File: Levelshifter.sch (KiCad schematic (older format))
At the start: 7 parts

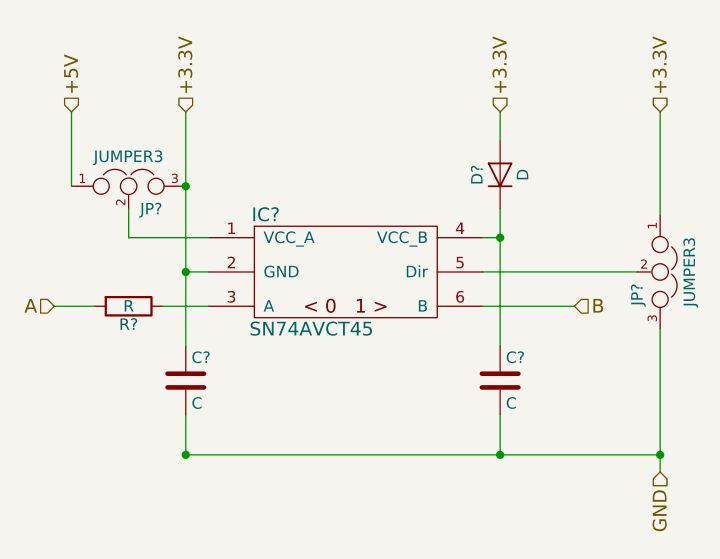
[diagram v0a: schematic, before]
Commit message: Route power, reroute data signals to top layer
Signed-off-by: katie dunne <kedunne@lbl.gov>
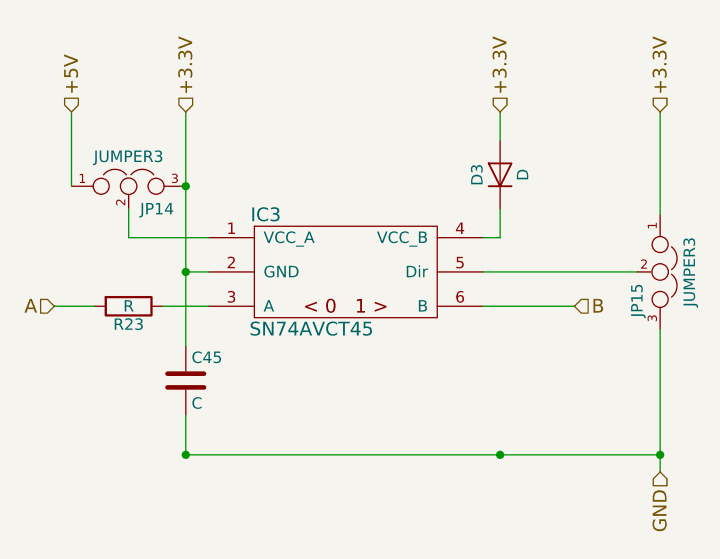
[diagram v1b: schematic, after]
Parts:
- removed C?: C, symbol C
- C43: renamed from C?; footprint (none) -> Capacitors_SMD:C_0805_HandSoldering
- D2: renamed from D?; footprint (none) -> Diodes_SMD:D_0805
- IC2: renamed from IC?; footprint (none) -> TO_SOT_Packages_SMD:SOT-23-6_Handsoldering
- R22: renamed from R?; footprint (none) -> Resistors_SMD:R_0603_HandSoldering
- gave numbers to parts that had none: 2
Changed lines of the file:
@@
 EESchema Schematic File Version 2
+LIBS:vhdci_fei4_rj45-rescue
+LIBS:ds90lv004
+LIBS:con-molex-vhdci
 LIBS:power
 LIBS:device
@@
 $EndDescr
 $Comp
-L JUMPER3 JP?
+L JUMPER3 JP16
 U 1 1 59136121
 P 3825 4150
-F 0 "JP?" H 3875 4050 50  0000 L CNN
+AR Path="/59195600/59136121" Ref="JP16"  Part="1"
+AR Path="/59133F97/59136121" Ref="JP14"  Part="1"
+AR Path="/5919615E/59136121" Ref="JP18"  Part="1"
+F 0 "JP14" H 3875 4050 50  0000 L CNN
 F 1 "JUMPER3" H 3825 4250 50  0000 C BNN
 F 2 "" H 3825 4150 50  0000 C CNN
@@
 $EndComp
 $Comp
-L JUMPER3 JP?
+L JUMPER3 JP17
 U 1 1 5913615C
 P 6150 4525
-F 0 "JP?" H 6200 4425 50  0000 L CNN
+AR Path="/59195600/5913615C" Ref="JP17"  Part="1"
+AR Path="/59133F97/5913615C" Ref="JP15"  Part="1"
+AR Path="/5919615E/5913615C" Ref="JP19"  Part="1"
+F 0 "JP15" H 6200 4425 50  0000 L CNN
 F 1 "JUMPER3" H 6150 4625 50  0000 C BNN
 F 2 "" H 6150 4525 50  0000 C CNN
@@
 $EndComp
 $Comp
-L C C?
+L C C43
 U 1 1 5913620E
 P 4075 5000
-F 0 "C?" H 4100 5100 50  0000 L CNN
+AR Path="/59195600/5913620E" Ref="C43"  Part="1"
+AR Path="/59133F97/5913620E" Ref="C41"  Part="1"
+AR Path="/5919615E/5913620E" Ref="C45"  Part="1"
+F 0 "C45" H 4100 5100 50  0000 L CNN
 F 1 "C" H 4100 4900 50  0000 L CNN
-F 2 "" H 4113 4850 50  0001 C CNN
+F 2 "Capacitors_SMD:C_0805_HandSoldering" H 4113 4850 50  0001 C CNN
 F 3 "" H 4075 5000 50  0001 C CNN
 	1    4075 5000
@@
 $EndComp
 $Comp
-L C C?
-U 1 1 5913623B
-P 5450 5000
-F 0 "C?" H 5475 5100 50  0000 L CNN
-F 1 "C" H 5475 4900 50  0000 L CNN
-F 2 "" H 5488 4850 50  0001 C CNN
-F 3 "" H 5450 5000 50  0001 C CNN
-	1    5450 5000
-	1    0    0    -1
-$EndComp
-$Comp
-L SN74AVCT45 IC?
+L SN74AVCT45 IC2
 U 1 1 591362B4
 P 4825 4525
-F 0 "IC?" H 4425 4775 60  0000 C CNN
+AR Path="/59195600/591362B4" Ref="IC2"  Part="1"
+AR Path="/59133F97/591362B4" Ref="IC1"  Part="1"
+AR Path="/5919615E/591362B4" Ref="IC3"  Part="1"
+F 0 "IC3" H 4425 4775 60  0000 C CNN
 F 1 "SN74AVCT45" H 4625 4275 60  0000 C CNN
-F 2 "" H 4175 4675 60  0001 C CNN
+F 2 "TO_SOT_Packages_SMD:SOT-23-6_Handsoldering" H 4175 4675 60  0001 C CNN
 F 3 "" H 4175 4675 60  0001 C CNN
 	1    4825 4525
@@
 $EndComp
 $Comp
-L R R?
+L R R22
 U 1 1 59136685
 P 3825 4675
-F 0 "R?" V 3905 4675 50  0000 C CNN
+AR Path="/59195600/59136685" Ref="R22"  Part="1"
+AR Path="/59133F97/59136685" Ref="R21"  Part="1"
+AR Path="/5919615E/59136685" Ref="R23"  Part="1"
+F 0 "R23" V 3905 4675 50  0000 C CNN
 F 1 "R" V 3825 4675 50  0000 C CNN
-F 2 "" V 3755 4675 50  0001 C CNN
+F 2 "Resistors_SMD:R_0603_HandSoldering" V 3755 4675 50  0001 C CNN
 F 3 "" H 3825 4675 50  0001 C CNN
 	1    3825 4675
@@
 A
 $Comp
-L D D?
+L D D2
 U 1 1 59136F14
 P 5450 4100
-F 0 "D?" H 5450 4200 50  0000 C CNN
+AR Path="/59195600/59136F14" Ref="D2"  Part="1"
+AR Path="/59133F97/59136F14" Ref="D1"  Part="1"
+AR Path="/5919615E/59136F14" Ref="D3"  Part="1"
+F 0 "D3" H 5450 4200 50  0000 C CNN
 F 1 "D" H 5450 4000 50  0000 C CNN
-F 2 "" H 5450 4100 50  0001 C CNN
+F 2 "Diodes_SMD:D_0805" H 5450 4100 50  0001 C CNN
 F 3 "" H 5450 4100 50  0001 C CNN
 	1    5450 4100
@@
 Wire Wire Line
 	5375 4375 5450 4375
-Connection ~ 5450 4375
-Wire Wire Line
-	5450 5150 5450 5325
 Connection ~ 5450 5325
-Wire Wire Line
-	5450 4250 5450 4850
 Wire Wire Line
 	5375 4525 6050 4525
@@
 	6150 4775 6150 5400
 Connection ~ 6150 5325
+Wire Wire Line
+	5450 4375 5450 4250
 $EndSCHEMATC

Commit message: Route U6, U4, U5
Signed-off-by: Katie Dunne <kdunne@mail.ccsf.edu>
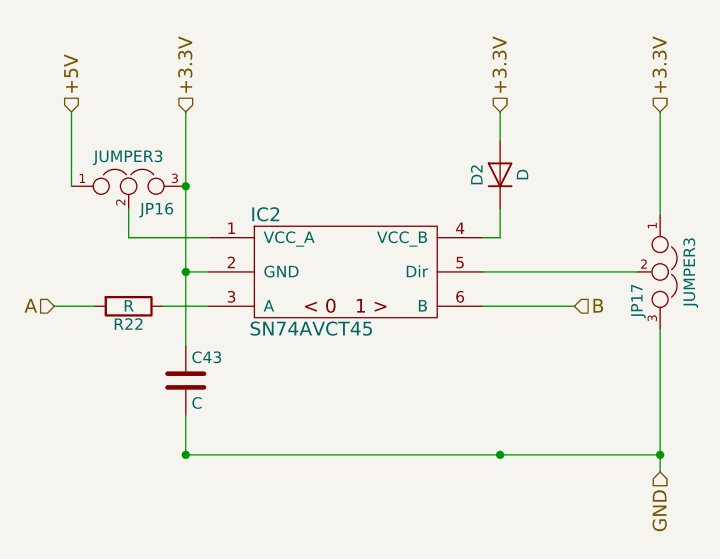
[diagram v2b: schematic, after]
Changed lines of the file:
@@
 EESchema Schematic File Version 2
 LIBS:vhdci_fei4_rj45-rescue
-LIBS:ds90lv004
-LIBS:con-molex-vhdci
 LIBS:power
 LIBS:device
@@
 LIBS:contrib
 LIBS:valves
-LIBS:module
 LIBS:vhdci_fei4_rj45-cache
 EELAYER 25 0
@@
 AR Path="/59133F97/59136121" Ref="JP14"  Part="1"
 AR Path="/5919615E/59136121" Ref="JP18"  Part="1"
-F 0 "JP14" H 3875 4050 50  0000 L CNN
+F 0 "JP16" H 3875 4050 50  0000 L CNN
 F 1 "JUMPER3" H 3825 4250 50  0000 C BNN
 F 2 "" H 3825 4150 50  0000 C CNN
@@
 AR Path="/59133F97/5913615C" Ref="JP15"  Part="1"
 AR Path="/5919615E/5913615C" Ref="JP19"  Part="1"
-F 0 "JP15" H 6200 4425 50  0000 L CNN
+F 0 "JP17" H 6200 4425 50  0000 L CNN
 F 1 "JUMPER3" H 6150 4625 50  0000 C BNN
 F 2 "" H 6150 4525 50  0000 C CNN
@@
 AR Path="/59133F97/5913620E" Ref="C41"  Part="1"
 AR Path="/5919615E/5913620E" Ref="C45"  Part="1"
-F 0 "C45" H 4100 5100 50  0000 L CNN
+F 0 "C43" H 4100 5100 50  0000 L CNN
 F 1 "C" H 4100 4900 50  0000 L CNN
 F 2 "Capacitors_SMD:C_0805_HandSoldering" H 4113 4850 50  0001 C CNN
@@
 AR Path="/59133F97/591362B4" Ref="IC1"  Part="1"
 AR Path="/5919615E/591362B4" Ref="IC3"  Part="1"
-F 0 "IC3" H 4425 4775 60  0000 C CNN
+F 0 "IC2" H 4425 4775 60  0000 C CNN
 F 1 "SN74AVCT45" H 4625 4275 60  0000 C CNN
 F 2 "TO_SOT_Packages_SMD:SOT-23-6_Handsoldering" H 4175 4675 60  0001 C CNN
@@
 AR Path="/59133F97/59136685" Ref="R21"  Part="1"
 AR Path="/5919615E/59136685" Ref="R23"  Part="1"
-F 0 "R23" V 3905 4675 50  0000 C CNN
+F 0 "R22" V 3905 4675 50  0000 C CNN
 F 1 "R" V 3825 4675 50  0000 C CNN
 F 2 "Resistors_SMD:R_0603_HandSoldering" V 3755 4675 50  0001 C CNN
@@
 AR Path="/59133F97/59136F14" Ref="D1"  Part="1"
 AR Path="/5919615E/59136F14" Ref="D3"  Part="1"
-F 0 "D3" H 5450 4200 50  0000 C CNN
+F 0 "D2" H 5450 4200 50  0000 C CNN
 F 1 "D" H 5450 4000 50  0000 C CNN
 F 2 "Diodes_SMD:D_0805" H 5450 4100 50  0001 C CNN

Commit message: Route 2 level shifters
Signed-off-by: katie dunne <kedunne@lbl.gov>
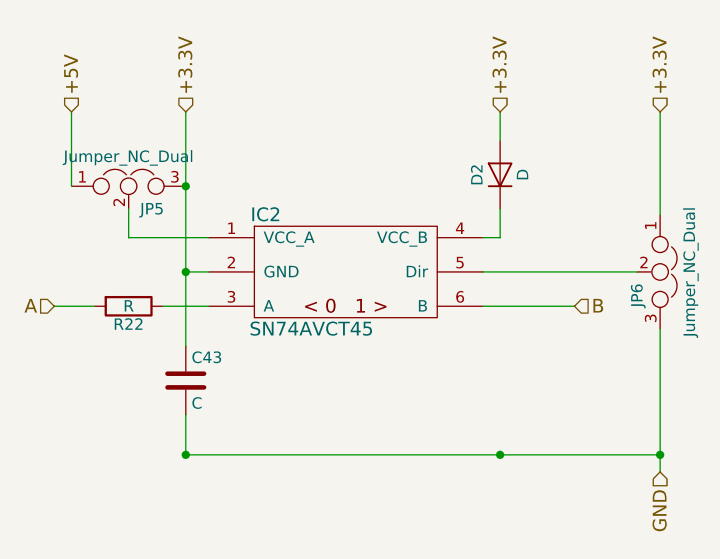
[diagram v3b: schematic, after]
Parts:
- removed JP16, JP17: JUMPER3, symbol JUMPER3
- added JP1, JP2: Jumper_NC_Dual, Connectors:GS3, symbol Jumper_NC_Dual
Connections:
- net +3.3V: now also JP1.3, JP2.1
- net +5V: now also JP1.1
- net GND: now also JP2.3
- net at IC2.1 (VCC_A): now also JP1.2
- net at IC2.5 (Dir): now also JP2.2
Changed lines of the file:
@@
 EESchema Schematic File Version 2
 LIBS:vhdci_fei4_rj45-rescue
+LIBS:ds90lv004
+LIBS:con-molex-vhdci
 LIBS:power
 LIBS:device
@@
 LIBS:contrib
 LIBS:valves
+LIBS:module
 LIBS:vhdci_fei4_rj45-cache
 EELAYER 25 0
@@
 $Descr A4 11693 8268
 encoding utf-8
-Sheet 9 10
+Sheet 10 10
 Title ""
 Date ""
@@
 Comment4 ""
 $EndDescr
-$Comp
-L JUMPER3 JP16
-U 1 1 59136121
-P 3825 4150
-AR Path="/59195600/59136121" Ref="JP16"  Part="1"
-AR Path="/59133F97/59136121" Ref="JP14"  Part="1"
-AR Path="/5919615E/59136121" Ref="JP18"  Part="1"
-F 0 "JP16" H 3875 4050 50  0000 L CNN
-F 1 "JUMPER3" H 3825 4250 50  0000 C BNN
-F 2 "" H 3825 4150 50  0000 C CNN
-F 3 "" H 3825 4150 50  0000 C CNN
-	1    3825 4150
-	1    0    0    -1
-$EndComp
-$Comp
-L JUMPER3 JP17
-U 1 1 5913615C
-P 6150 4525
-AR Path="/59195600/5913615C" Ref="JP17"  Part="1"
-AR Path="/59133F97/5913615C" Ref="JP15"  Part="1"
-AR Path="/5919615E/5913615C" Ref="JP19"  Part="1"
-F 0 "JP17" H 6200 4425 50  0000 L CNN
-F 1 "JUMPER3" H 6150 4625 50  0000 C BNN
-F 2 "" H 6150 4525 50  0000 C CNN
-F 3 "" H 6150 4525 50  0000 C CNN
-	1    6150 4525
-	0    1    1    0
-$EndComp
 $Comp
 L C C43
@@
 Wire Wire Line
 	5450 4375 5450 4250
+$Comp
+L Jumper_NC_Dual JP1
+U 1 1 591A2FEC
+P 3825 4150
+AR Path="/59133F97/591A2FEC" Ref="JP1"  Part="1"
+AR Path="/5919615E/591A2FEC" Ref="JP3"  Part="1"
+AR Path="/59195600/591A2FEC" Ref="JP5"  Part="1"
+F 0 "JP5" H 3875 4050 50  0000 L CNN
+F 1 "Jumper_NC_Dual" H 3825 4250 50  0000 C BNN
+F 2 "Connectors:GS3" H 3825 4150 50  0001 C CNN
+F 3 "" H 3825 4150 50  0001 C CNN
+	1    3825 4150
+	1    0    0    -1
+$EndComp
+$Comp
+L Jumper_NC_Dual JP2
+U 1 1 591A318A
+P 6150 4525
+AR Path="/59133F97/591A318A" Ref="JP2"  Part="1"
+AR Path="/5919615E/591A318A" Ref="JP4"  Part="1"
+AR Path="/59195600/591A318A" Ref="JP6"  Part="1"
+F 0 "JP6" H 6200 4425 50  0000 L CNN
+F 1 "Jumper_NC_Dual" H 6150 4625 50  0000 C BNN
+F 2 "Connectors:GS3" H 6150 4525 50  0001 C CNN
+F 3 "" H 6150 4525 50  0001 C CNN
+	1    6150 4525
+	0    1    1    0
+$EndComp
 $EndSCHEMATC
